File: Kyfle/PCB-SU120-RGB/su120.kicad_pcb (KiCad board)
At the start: 2 copper layers, 98 x 98 mm, 450 parts, among them J1 MJ-4PP-9, J2 Conn_01x03, J3 Conn_01x08, J4 Conn_01x08, J5 Conn_01x03, J6 MJ-4PP-9, J7 Conn_02x05_Odd_Even, J8 Conn_02x05_Odd_Even, SW1 SW_PUSH_LED, SW10 SW_PUSH_LED, SW11 SW_PUSH_LED, SW12 SW_PUSH_LED, SW13 SW_PUSH_LED, SW14 SW_PUSH_LED, SW15 SW_PUSH_LED, SW16 SW_PUSH_LED, SW17 SW_PUSH_LED, SW18 SW_PUSH_LED, SW19 LED_SK6812_Mini_E, SW2 SW_PUSH_LED, SW20 Rotary_Encoder_Switch, SW21 Rotary_Encoder_Switch, SW22 SW_Push, SW23 LED_SK6812_Mini_E, SW24 LED_SK6812_Mini_E, SW3 SW_PUSH_LED, SW4 SW_PUSH_LED, SW5 SW_PUSH_LED, SW6 SW_PUSH_LED, SW7 SW_PUSH_LED, SW8 SW_PUSH_LED, SW9 SW_PUSH_LED, U1 ProMicro

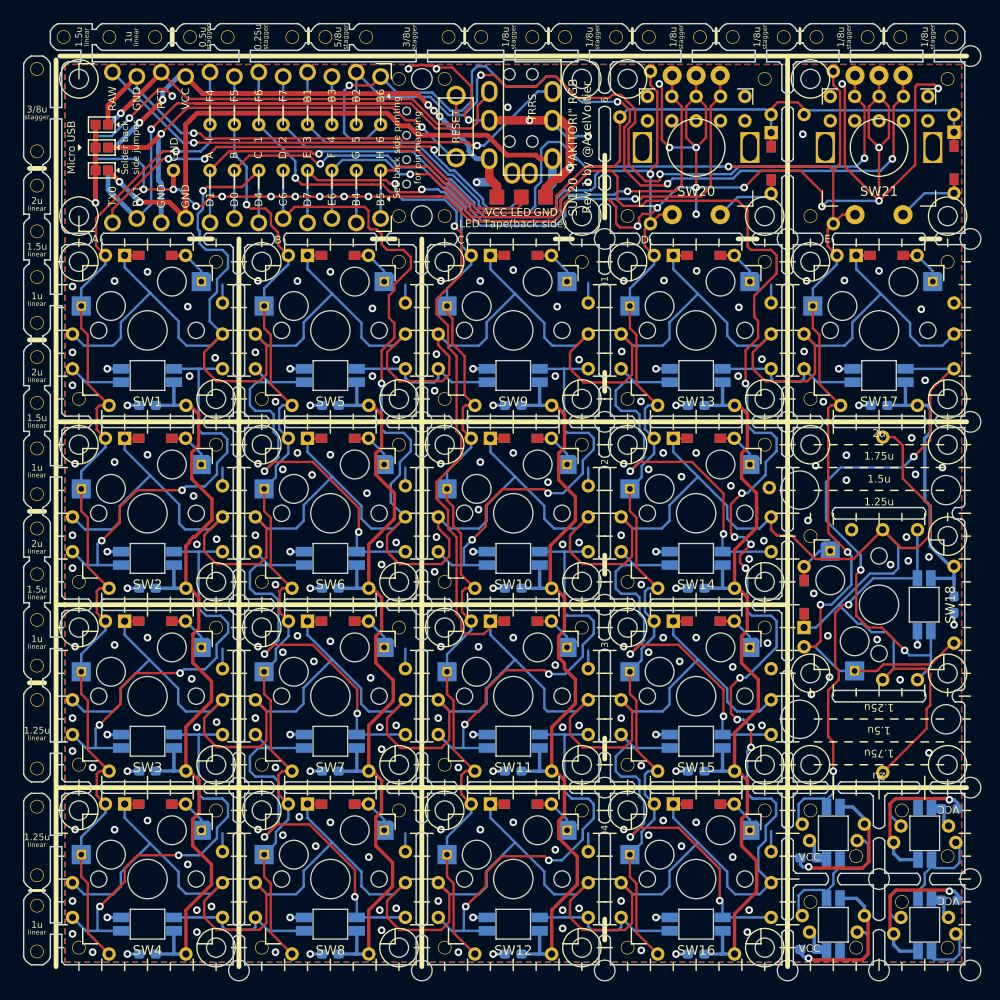
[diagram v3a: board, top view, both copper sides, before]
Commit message: Fixuturing solution for the pro micro board
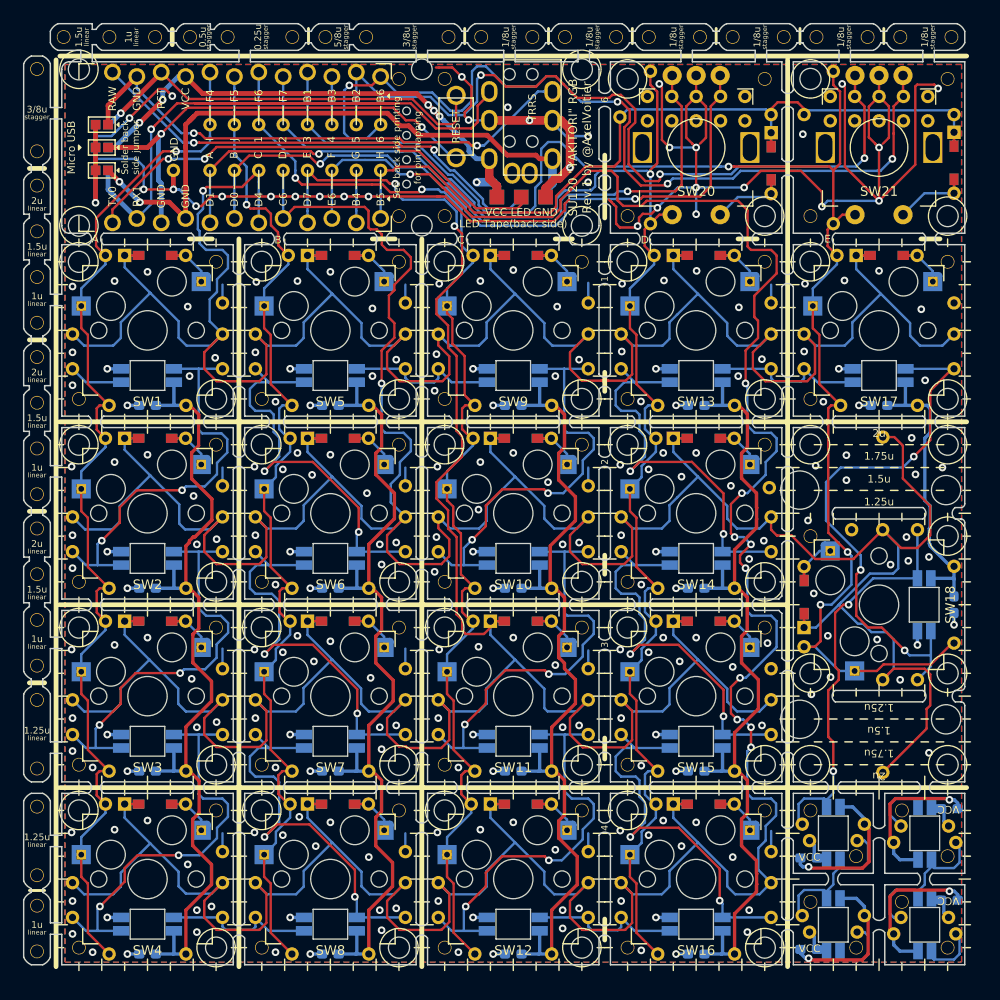
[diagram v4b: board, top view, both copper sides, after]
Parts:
- removed the ? at (127.8, 142.9)
- removed the ? at (137.3, 57.2)
- removed the ? at (137.3, 95.2)
- removed the ? at (99.2, 152.4)
- removed the ? at (99.2, 133.3)
- removed the ? at (80.2, 133.3)
- removed the ? at (61.1, 133.3)
- removed the ? at (137.3, 76.2)
- removed the ? at (137.3, 152.4)
- removed the ? at (99.2, 76.2)
- removed the ? at (118.3, 95.3)
- removed the ? at (80.2, 152.4)
- removed the ? at (61.1, 152.4)
- removed the ? at (99.2, 114.3)
- removed the ? at (80.2, 114.3)
- removed the ? at (61.1, 114.3)
- removed the ? at (80.2, 95.3)
- removed the ? at (99.2, 95.3)
- removed the ? at (118.3, 76.2)
- removed the ? at (127.8, 152.4)
- removed the ? at (137.3, 142.9)
- removed the ? at (137.3, 133.3)
- removed the ? at (118.3, 133.3)
- removed the ? at (118.3, 152.4)
- removed the ? at (61.1, 95.3)
- moved ? 1.00 mm to (80.2, 58.5)
- moved ? 1.00 mm to (80.2, 74.8)
- moved ? 1.00 mm to (96.8, 58.5)
- moved ? 1.00 mm to (96.8, 74.8)
- moved ? 1.00 mm to (44.5, 58.5)
- moved ? 1.00 mm to (44.5, 74.8)
- moved H115 0.19 mm to (85.5, 116.0)
- moved H22 0.19 mm to (66.5, 97.0)
- moved H116 0.19 mm to (104.6, 116.0)
- moved H117 0.19 mm to (66.5, 135.1)
- moved H23 0.19 mm to (85.5, 97.0)
- moved H24 0.19 mm to (104.6, 97.0)
- moved H3 0.19 mm to (85.5, 77.9)
- moved H42 0.17 mm to (104.6, 135.1)
- moved H114 0.17 mm to (66.5, 116.0)
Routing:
- net GND: track 391.0 -> 387.9 mm, vias 246 -> 245
- net X3: track 132.1 -> 132.9 mm
- net X4: track 171.8 -> 172.6 mm
- net X2: track 119.5 -> 120.3 mm
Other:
- outline, holes or cut-outs redrawn

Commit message: Reorganising the pro micro bit board
- Changed how the jumper selectors work (the ones needed for reversible usage of the board)
- As it maded more space, I increased even more the power delivery for LED use case
- Changed footprint of OLED connector. Instead of just being through holes, they are now solderable through holes (though not connected to anything). It should help for mechanical stability of the screen.
- Small changes to hole sizes
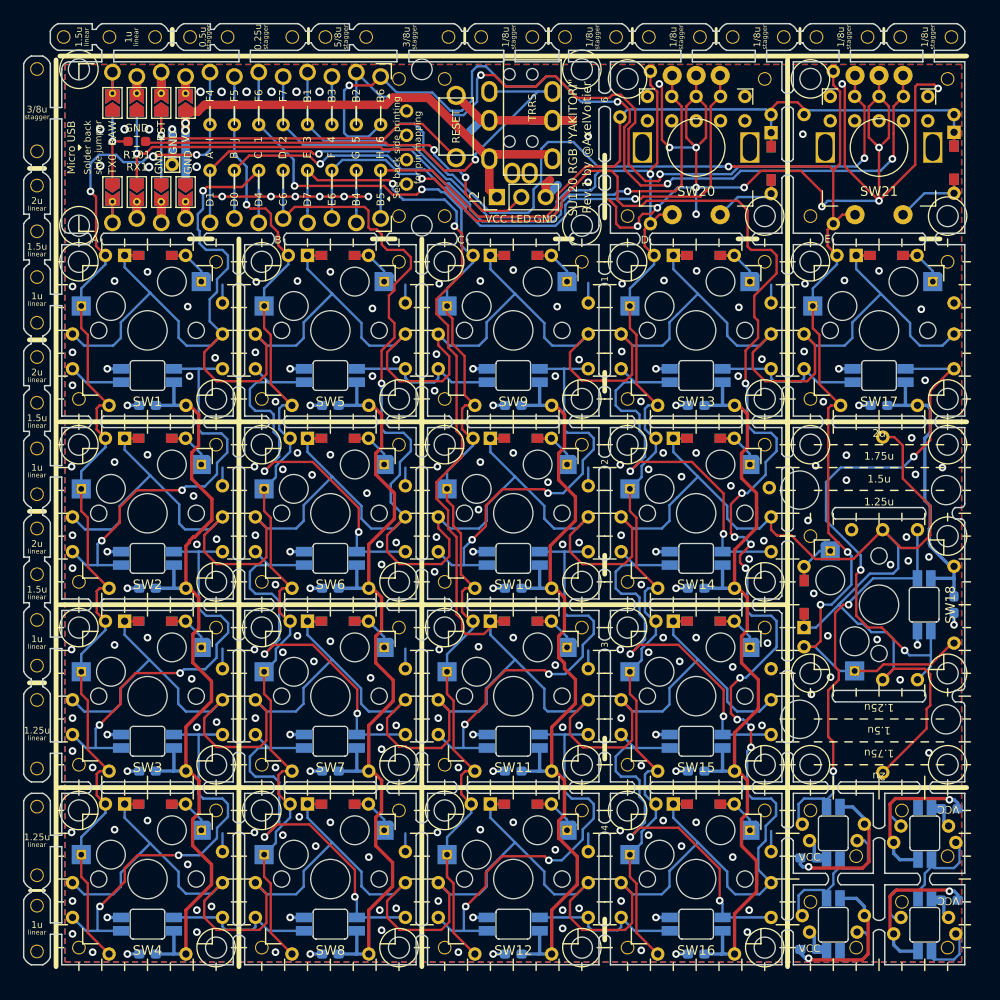
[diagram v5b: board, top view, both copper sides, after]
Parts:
- removed J5: Conn_01x03, #footprint:StripLED_rev2
- removed JP1, JP2, JP3, JP4, JP5, JP6: SolderJumper_2_Open, #footprint:SolderJumper-2_P1.3mm_Open_Pad1.0x1.0mm
- added JP101: SolderJumper_3_Open, #footprint:SolderJumper-3_P1.3mm_Open_TrianglePad1.0x1.5mm_duplex, B.Cu at (55.6, 62.2)
- added JP102: SolderJumper_3_Open, #footprint:SolderJumper-3_P1.3mm_Open_TrianglePad1.0x1.5mm_duplex, B.Cu at (53.0, 62.2)
- added JP103: SolderJumper_3_Open, #footprint:SolderJumper-3_P1.3mm_Open_TrianglePad1.0x1.5mm_duplex, B.Cu at (50.5, 62.2)
- added JP104: SolderJumper_3_Open, #footprint:SolderJumper-3_P1.3mm_Open_TrianglePad1.0x1.5mm_duplex, B.Cu at (47.9, 62.2)
- added JP105: SolderJumper_3_Open, #footprint:SolderJumper-3_P1.3mm_Open_TrianglePad1.0x1.5mm_duplex, B.Cu at (47.9, 71.1)
- added JP106: SolderJumper_3_Open, #footprint:SolderJumper-3_P1.3mm_Open_TrianglePad1.0x1.5mm_duplex, B.Cu at (50.5, 71.1)
- added JP107: SolderJumper_3_Open, #footprint:SolderJumper-3_P1.3mm_Open_TrianglePad1.0x1.5mm_duplex, B.Cu at (53.0, 71.1)
- added JP108: SolderJumper_3_Open, #footprint:SolderJumper-3_P1.3mm_Open_TrianglePad1.0x1.5mm_duplex, B.Cu at (55.6, 71.1)
- added R101: 50R, Resistor_SMD:R_0603_1608Metric_Pad0.98x0.95mm_HandSolder, F.Cu at (50.5, 66.0)
- ?: footprint #footprint:OLED_Hole -> #footprint:OLED
- J2: footprint #footprint:StripLED_rev2 -> Connector_PinHeader_2.54mm:PinHeader_1x03_P2.54mm_Vertical
- moved H57 0.62 mm to (54.2, 68.5)
- renumbered SW?1 to LED1, SW19 to LED2, SW23 to LED3, SW24 to LED4
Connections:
- J2 pad 2: led -> Net-(J2-Pad2)
- J6 pad B: dummydata -> data
- J6 pad D: dummyVCC -> VCC
- SW22 pad 2: reset2 -> GND
- U1 pad 1: led -> Net-(JP104-Pad2)
- U1 pad 2: data -> Net-(JP103-Pad2)
- U1 pad 21: VCC -> Net-(JP108-Pad2)
- U1 pad 22: reset1 -> Net-(JP107-Pad2)
- U1 pad 23: dummydata -> Net-(JP106-Pad2)
- U1 pad 24: dummyled -> Net-(JP105-Pad2)
- U1 pad 3: reset2 -> Net-(JP102-Pad2)
- U1 pad 4: dummyVCC -> Net-(JP101-Pad2)
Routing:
- net GND: track 387.9 -> 302.9 mm, vias 245 -> 246
- net dummydata: track 77.2 -> 0.00 mm, vias 1 -> 0
- net dummyVCC: track 55.3 -> 0.00 mm, vias 5 -> 0
- net dummyled: track 50.1 -> 0.00 mm, vias 2 -> 0
- net Net-(J2-Pad2): track 0.00 -> 44.0 mm, vias 0 -> 2
- net reset2: track 43.7 -> 0.00 mm, vias 1 -> 0
- net led: track 49.5 -> 9.07 mm, vias 2 -> 1
- net VCC: track 461.9 -> 451.2 mm
- net reset1: track 50.3 -> 40.4 mm, vias 2 -> 1
- net Net-(JP105-Pad2): track 0.00 -> 5.36 mm
- net data: track 56.5 -> 61.8 mm
- net X1: track 122.8 -> 127.9 mm, vias 1 -> 3
- net Net-(JP107-Pad2): track 0.00 -> 4.41 mm
- net Net-(JP104-Pad2): track 0.00 -> 4.41 mm
- net Net-(JP102-Pad2): track 0.00 -> 4.41 mm
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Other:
- outline, holes or cut-outs redrawn
- board text added: "SU120 RGB "YAKITORI" Rev.1 by @AxelVoitier"
- board text removed: "LED Tape(back side)"
- board text removed: "SU120 "YAKITORI" RGB Rev.1 by @AxelVoitier"
